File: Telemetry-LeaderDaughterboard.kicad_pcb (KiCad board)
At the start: 2 copper layers, 28 parts, among them J1 GPS_LogicAnalyzer, J2 SDCard_LogicAnalyzer, J3 Micro_SD_Card_Det, J4 SMAConn, SW1 SW_Push, SW2 SW_Push, SW3 SW_Push, SW4 SW_Push, SW5 SW_DIP_x04, U1 MTK3339

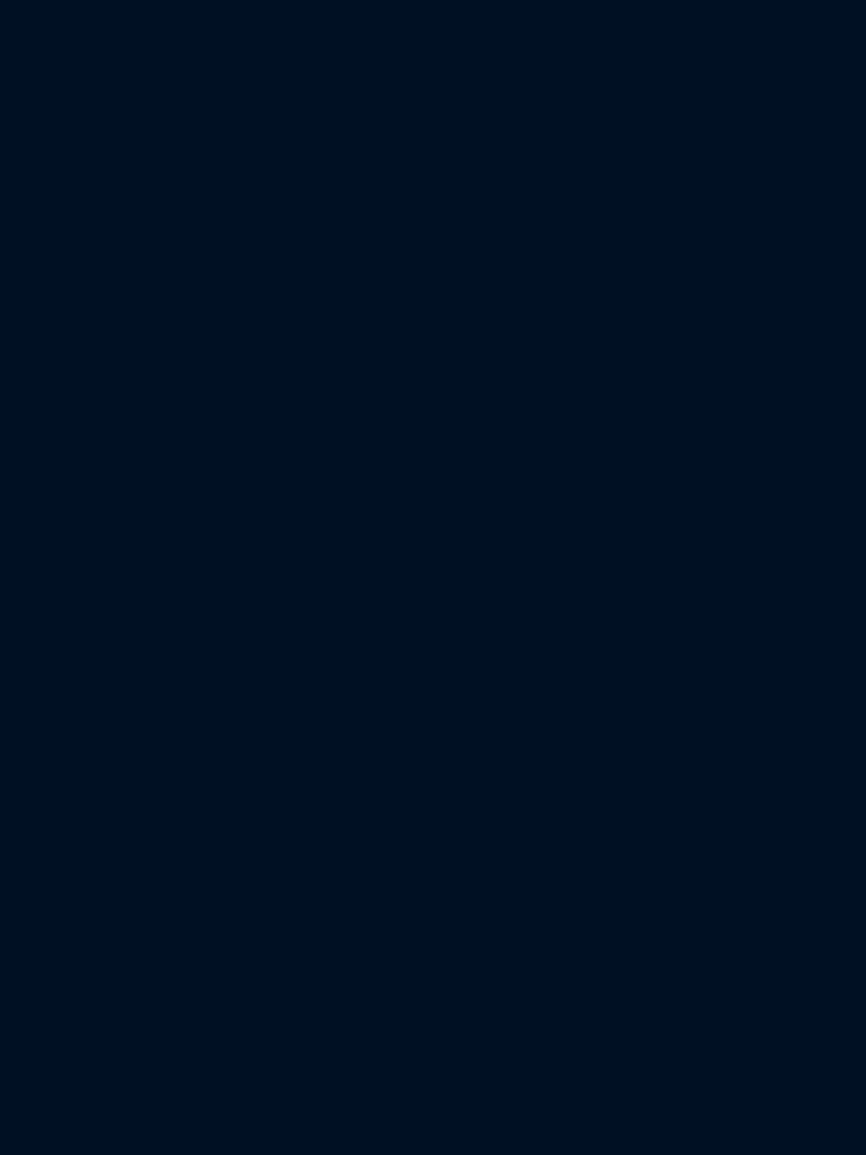
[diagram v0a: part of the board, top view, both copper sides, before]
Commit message: xbee initial addition
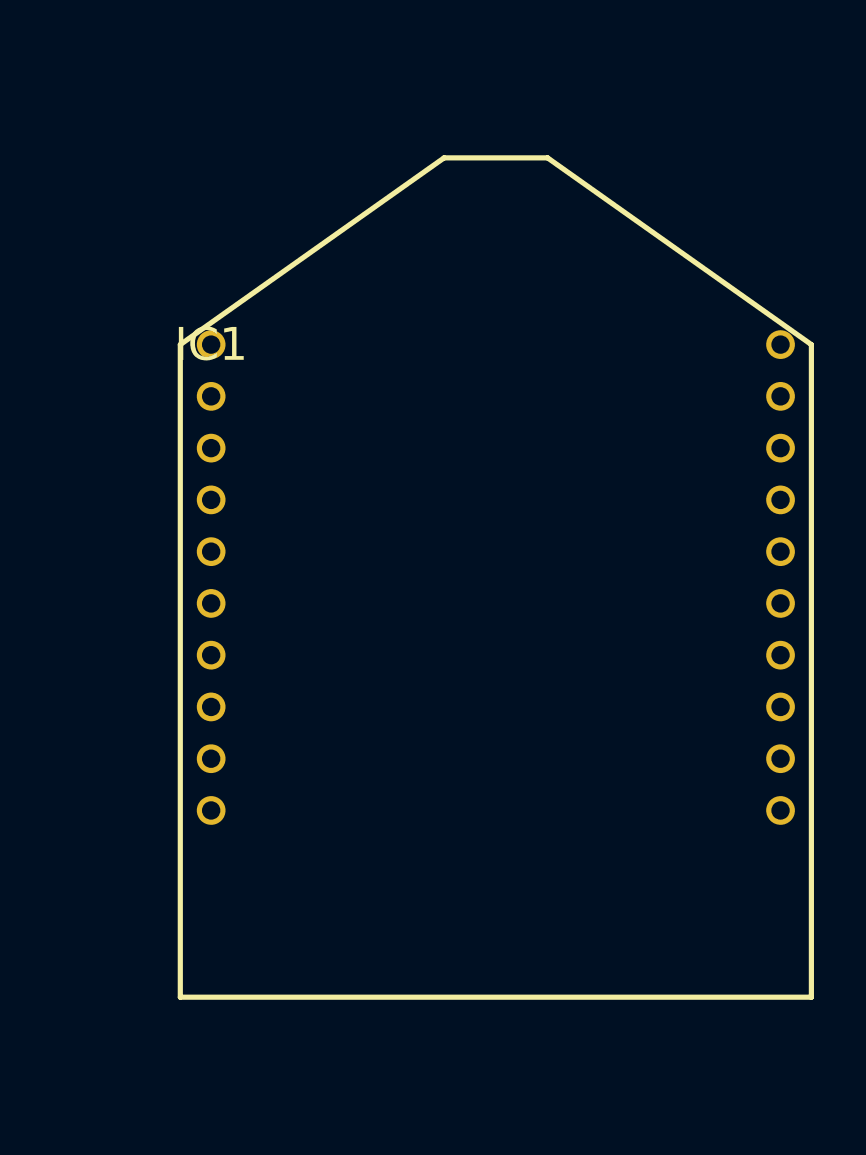
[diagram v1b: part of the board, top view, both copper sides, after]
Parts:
- added IC1: XBP9B-DMST-002, UTSVT_ICs:XBP9B-DMST-002, F.Cu at (185.0, 84.0)
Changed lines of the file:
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@@
   (net 41 "unconnected-(U1-NC-Pad18)")
   (net 42 "unconnected-(U1-NC-Pad20)")
+  (net 43 "unconnected-(IC1-Pad1)")
+  (net 44 "unconnected-(IC1-Pad2)")
+  (net 45 "unconnected-(IC1-Pad3)")
+  (net 46 "unconnected-(IC1-Pad4)")
+  (net 47 "unconnected-(IC1-Pad5)")
+  (net 48 "unconnected-(IC1-Pad6)")
+  (net 49 "unconnected-(IC1-Pad7)")
+  (net 50 "unconnected-(IC1-Pad8)")
+  (net 51 "unconnected-(IC1-Pad9)")
+  (net 52 "unconnected-(IC1-Pad10)")
+  (net 53 "unconnected-(IC1-Pad11)")
+  (net 54 "unconnected-(IC1-Pad12)")
+  (net 55 "unconnected-(IC1-Pad13)")
+  (net 56 "unconnected-(IC1-Pad14)")
+  (net 57 "unconnected-(IC1-Pad15)")
+  (net 58 "unconnected-(IC1-Pad16)")
+  (net 59 "unconnected-(IC1-Pad17)")
+  (net 60 "unconnected-(IC1-Pad18)")
+  (net 61 "unconnected-(IC1-Pad19)")
+  (net 62 "unconnected-(IC1-Pad20)")
   (footprint "Capacitor_SMD:C_0805_2012Metric" (layer "F.Cu")
     (at 128.85 93.95)
@@
     )
   )
+  (footprint "UTSVT_ICs:XBP9B-DMST-002" (layer "F.Cu")
+    (at 185 84)
+    (descr "XBee-PRO 900HP")
+    (tags "Integrated Circuit")
+    (property "Height" "")
+    (property "Manufacturer_Name" "Digi International")
+    (property "Manufacturer_Part_Number" "XBP9B-DMST-002")
+    (property "Mouser Part Number" "888-XBP9B-DMST-002")
+    (property "Mouser Price/Stock" "https://www.mouser.com/Search/Refine.aspx?Keyword=888-XBP9B-DMST-002")
+    (property "Sheetfile" "XBee.kicad_sch")
+    (property "Sheetname" "XBee")
+    (property "ki_description" "MODULE XBEE PRO S3B 900HP RPSMA")
+    (attr through_hole)
+    (fp_text reference "IC1" (at 0 0) (layer "F.SilkS")
+        (effects (font (size 1.27 1.27) (thickness 0.254)))
+    )
+    (fp_text value "XBP9B-DMST-002" (at 0 0) (layer "F.SilkS") hide
+        (effects (font (size 1.27 1.27) (thickness 0.254)))
+    )
+    (fp_text user "${REFERENCE}" (at 0 0) (layer "F.Fab")
+        (effects (font (size 1.27 1.27) (thickness 0.254)))
+    )
+    (fp_line (start -1.192 0) (end -1.192 25.215)
+      (stroke (width 0.2) (type solid)) (layer "F.SilkS"))
+    (fp_line (start -1.192 25.215) (end 23.192 25.215)
+      (stroke (width 0.2) (type solid)) (layer "F.SilkS"))
+    (fp_line (start 9 -7.215) (end -1.192 0)
+      (stroke (width 0.2) (type solid)) (layer "F.SilkS"))
+    (fp_line (start 13 -7.215) (end 9 -7.215)
+      (stroke (width 0.2) (type solid)) (layer "F.SilkS"))
+    (fp_line (start 23.192 0) (end 13 -7.215)
+      (stroke (width 0.2) (type solid)) (layer "F.SilkS"))
+    (fp_line (start 23.192 25.215) (end 23.192 0)
+      (stroke (width 0.2) (type solid)) (layer "F.SilkS"))
+    (fp_line (start -1.192 0) (end -1.192 25.215)
+      (stroke (width 0.2) (type solid)) (layer "F.Fab"))
+    (fp_line (start -1.192 25.215) (end 23.192 25.215)
+      (stroke (width 0.2) (type solid)) (layer "F.Fab"))
+    (fp_line (start 9 -7.215) (end -1.192 0)
+      (stroke (width 0.2) (type solid)) (layer "F.Fab"))
+    (fp_line (start 13 -7.215) (end 9 -7.215)
+      (stroke (width 0.2) (type solid)) (layer "F.Fab"))
+    (fp_line (start 23.192 0) (end 13 -7.215)
+      (stroke (width 0.2) (type solid)) (layer "F.Fab"))
+    (fp_line (start 23.192 25.215) (end 23.192 0)
+      (stroke (width 0.2) (type solid)) (layer "F.Fab"))
+    (pad "1" thru_hole circle (at 0 0) (size 1.11 1.11) (drill 0.71) (layers "*.Cu" "*.Mask")
+      (net 43 "unconnected-(IC1-Pad1)") (pinfunction "1") (pintype "passive"))
+    (pad "2" thru_hole circle (at 0 2) (size 1.11 1.11) (drill 0.71) (layers "*.Cu" "*.Mask")
+      (net 44 "unconnected-(IC1-Pad2)") (pinfunction "2") (pintype "passive"))
+    (pad "3" thru_hole circle (at 0 4) (size 1.11 1.11) (drill 0.71) (layers "*.Cu" "*.Mask")
+      (net 45 "unconnected-(IC1-Pad3)") (pinfunction "3") (pintype "passive"))
+    (pad "4" thru_hole circle (at 0 6) (size 1.11 1.11) (drill 0.71) (layers "*.Cu" "*.Mask")
+      (net 46 "unconnected-(IC1-Pad4)") (pinfunction "4") (pintype "passive"))
+    (pad "5" thru_hole circle (at 0 8) (size 1.11 1.11) (drill 0.71) (layers "*.Cu" "*.Mask")
+      (net 47 "unconnected-(IC1-Pad5)") (pinfunction "5") (pintype "passive"))
+    (pad "6" thru_hole circle (at 0 10) (size 1.11 1.11) (drill 0.71) (layers "*.Cu" "*.Mask")
+      (net 48 "unconnected-(IC1-Pad6)") (pinfunction "6") (pintype "passive"))
+    (pad "7" thru_hole circle (at 0 12) (size 1.11 1.11) (drill 0.71) (layers "*.Cu" "*.Mask")
+      (net 49 "unconnected-(IC1-Pad7)") (pinfunction "7") (pintype "passive"))
+    (pad "8" thru_hole circle (at 0 14) (size 1.11 1.11) (drill 0.71) (layers "*.Cu" "*.Mask")
+      (net 50 "unconnected-(IC1-Pad8)") (pinfunction "8") (pintype "passive"))
+    (pad "9" thru_hole circle (at 0 16) (size 1.11 1.11) (drill 0.71) (layers "*.Cu" "*.Mask")
+      (net 51 "unconnected-(IC1-Pad9)") (pinfunction "9") (pintype "passive"))
+    (pad "10" thru_hole circle (at 0 18) (size 1.11 1.11) (drill 0.71) (layers "*.Cu" "*.Mask")
+      (net 52 "unconnected-(IC1-Pad10)") (pinfunction "10") (pintype "passive"))
+    (pad "11" thru_hole circle (at 22 18) (size 1.11 1.11) (drill 0.71) (layers "*.Cu" "*.Mask")
+      (net 53 "unconnected-(IC1-Pad11)") (pinfunction "11") (pintype "passive"))
+    (pad "12" thru_hole circle (at 22 16) (size 1.11 1.11) (drill 0.71) (layers "*.Cu" "*.Mask")
+      (net 54 "unconnected-(IC1-Pad12)") (pinfunction "12") (pintype "passive"))
+    (pad "13" thru_hole circle (at 22 14) (size 1.11 1.11) (drill 0.71) (layers "*.Cu" "*.Mask")
+      (net 55 "unconnected-(IC1-Pad13)") (pinfunction "13") (pintype "passive"))
+    (pad "14" thru_hole circle (at 22 12) (size 1.11 1.11) (drill 0.71) (layers "*.Cu" "*.Mask")
+      (net 56 "unconnected-(IC1-Pad14)") (pinfunction "14") (pintype "passive"))
+    (pad "15" thru_hole circle (at 22 10) (size 1.11 1.11) (drill 0.71) (layers "*.Cu" "*.Mask")
+      (net 57 "unconnected-(IC1-Pad15)") (pinfunction "15") (pintype "passive"))
+    (pad "16" thru_hole circle (at 22 8) (size 1.11 1.11) (drill 0.71) (layers "*.Cu" "*.Mask")
+      (net 58 "unconnected-(IC1-Pad16)") (pinfunction "16") (pintype "passive"))
+    (pad "17" thru_hole circle (at 22 6) (size 1.11 1.11) (drill 0.71) (layers "*.Cu" "*.Mask")
+      (net 59 "unconnected-(IC1-Pad17)") (pinfunction "17") (pintype "passive"))
+    (pad "18" thru_hole circle (at 22 4) (size 1.11 1.11) (drill 0.71) (layers "*.Cu" "*.Mask")
+      (net 60 "unconnected-(IC1-Pad18)") (pinfunction "18") (pintype "passive"))
+    (pad "19" thru_hole circle (at 22 2) (size 1.11 1.11) (drill 0.71) (layers "*.Cu" "*.Mask")
+      (net 61 "unconnected-(IC1-Pad19)") (pinfunction "19") (pintype "passive"))
+    (pad "20" thru_hole circle (at 22 0) (size 1.11 1.11) (drill 0.71) (layers "*.Cu" "*.Mask")
+      (net 62 "unconnected-(IC1-Pad20)") (pinfunction "20") (pintype "passive"))
+    (model "${KIPRJMOD}/UTSVT-KiCadLibraries/utsvt3d/chips.3dshapes/XBPro-whip.STEP"
+      (offset (xyz -27.3 -14.3 40))
+      (scale (xyz 1 1 1))
+      (rotate (xyz 90 0 180))
+    )
+  )
